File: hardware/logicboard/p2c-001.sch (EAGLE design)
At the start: 44 parts, among them IC1 74LS07N, K1 G5V1, T1 2SC1815

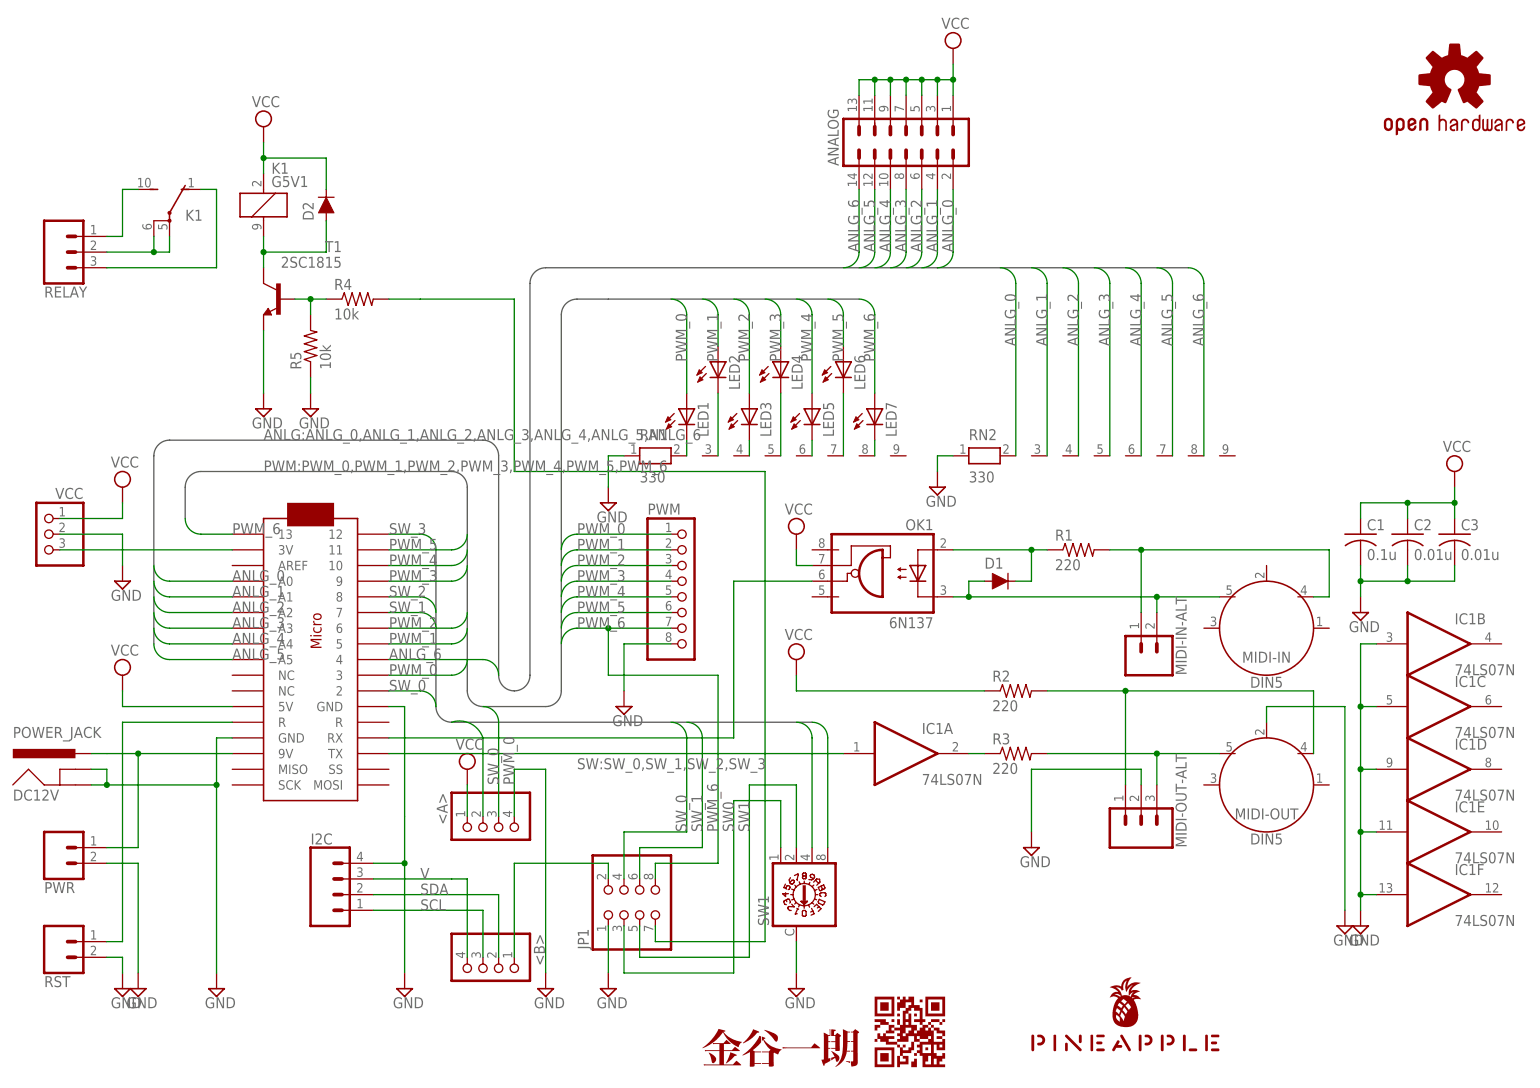
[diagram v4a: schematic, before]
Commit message: Changed DC jack and alternative connectors.
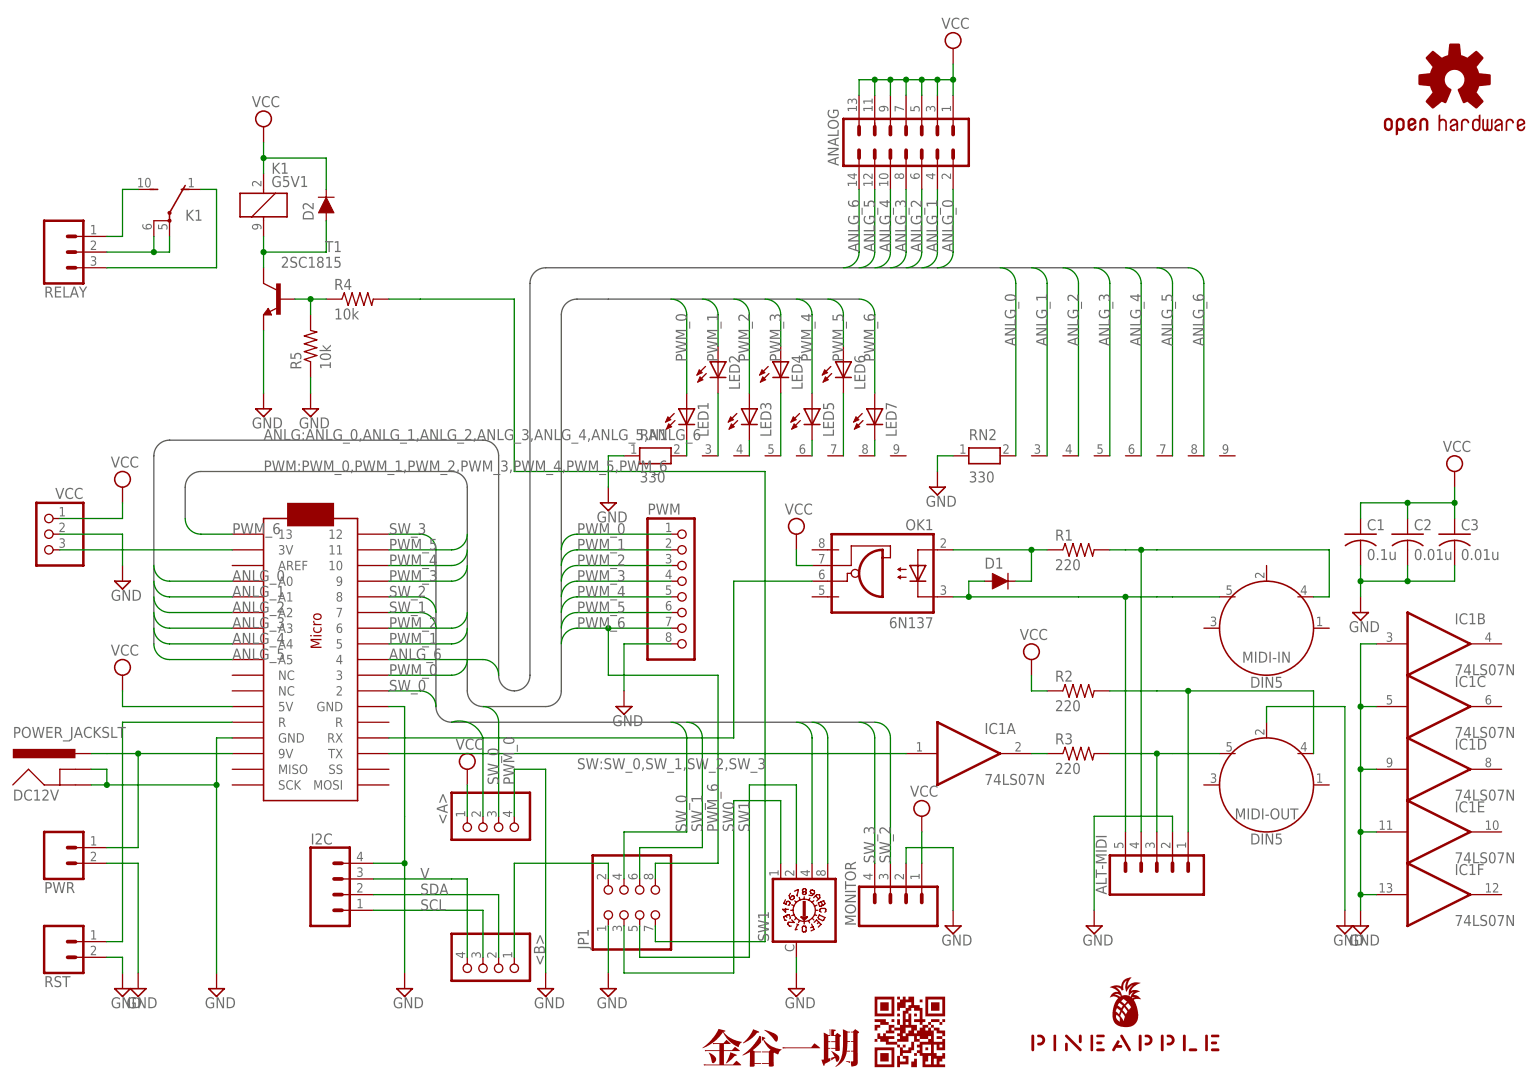
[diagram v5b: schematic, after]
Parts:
- removed MIDI-IN-ALT: (no value), SparkFun-Connectors:CONN_02JST-PTH-2
- removed MIDI-OUT-ALT: (no value), SparkFun-Connectors:CONN_03JST-PTH
- added ALT-MIDI: (no value), SparkFun-Connectors:CONN_05JST
- added MONITOR: (no value), SparkFun-Connectors:CONN_041.27MM
- DC12V: value POWER_JACK -> POWER_JACKSLT; device SparkFun-Connectors:POWER_JACK -> SparkFun-Connectors:POWER_JACKSLT
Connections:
- net GND: now also ALT-MIDI.2, MONITOR.2; no longer MIDI-OUT-ALT.2
- net MIDIIN+: now also ALT-MIDI.4; no longer MIDI-IN-ALT.1
- net MIDIIN-: now also ALT-MIDI.5; no longer MIDI-IN-ALT.2
- net MIDIOUT+: now also ALT-MIDI.1; no longer MIDI-OUT-ALT.1
- net MIDIOUT-: now also ALT-MIDI.3; no longer MIDI-OUT-ALT.3
- net SW_2: now also MONITOR.3
- net SW_3: now also MONITOR.4
- net VCC: now also MONITOR.1
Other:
- moved on the sheet: IC1A, R2, R3, SW1

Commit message: GND pad.
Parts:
- added GND: (no value), pinhead:PINHD-2X4
- MONITOR: device SparkFun-Connectors:CONN_041.27MM -> SparkFun-Connectors:CONN_04JST-PTH-VERT
- renumbered LED1 to L1, LED2 to L2, LED3 to L3, LED4 to L4, LED5 to L5, LED6 to L6, LED7 to L7
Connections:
- net GND: now also GND.1, GND.2, GND.3, GND.4, GND.5, GND.6, GND.7, GND.8
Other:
- moved on the sheet: C1, C2, C3

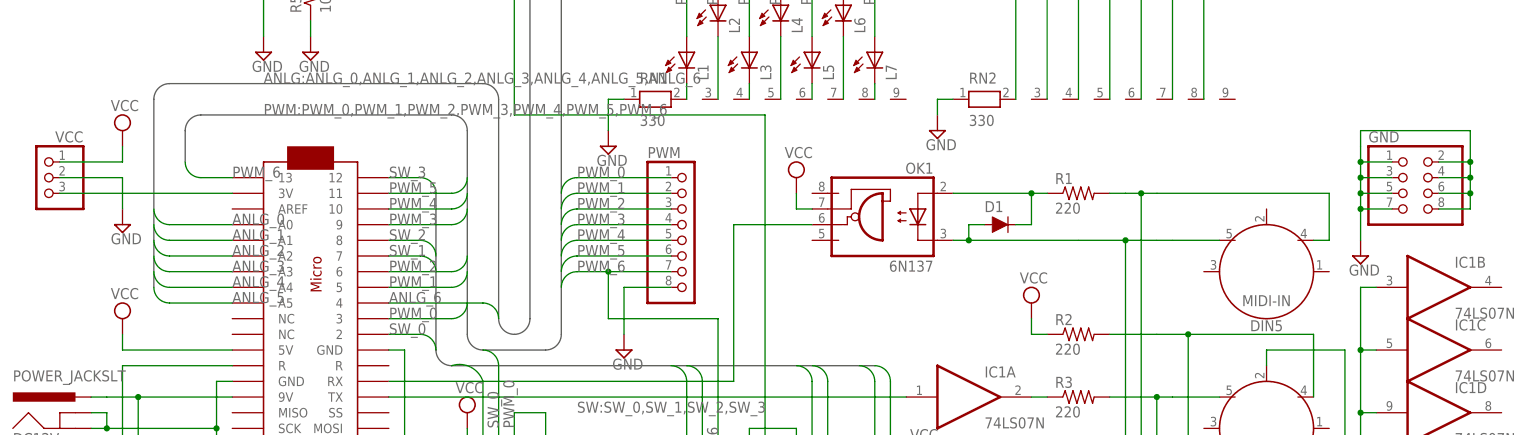
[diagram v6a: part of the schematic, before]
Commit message: Changed pinheaders to Sparkfan's ones.
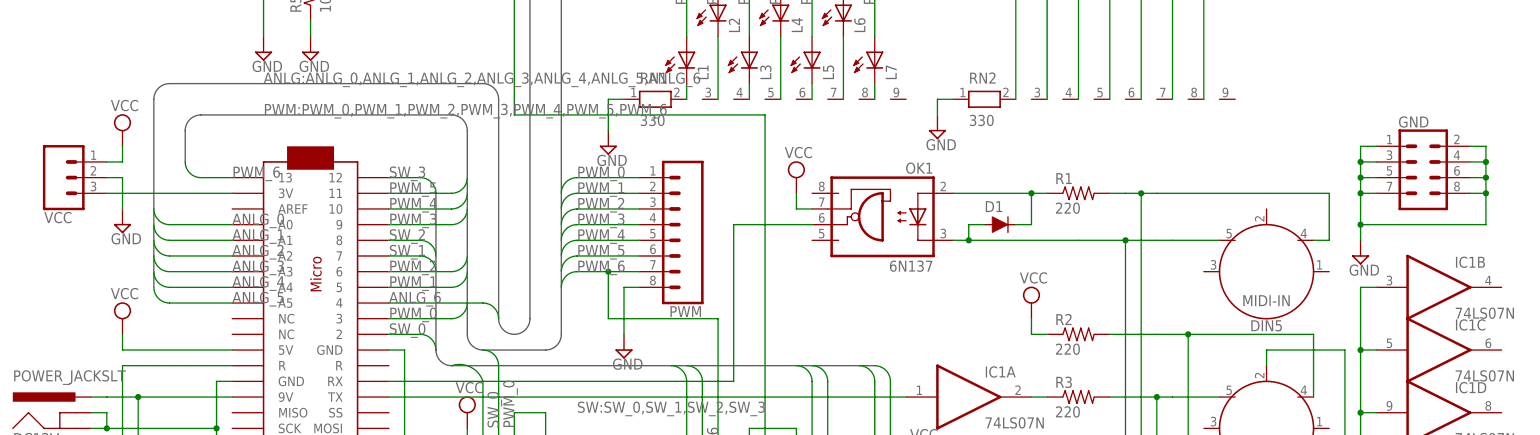
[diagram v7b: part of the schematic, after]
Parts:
- GND: device pinhead:PINHD-2X4 -> SparkFun-Connectors:CONN_04X2
- PWM: device pinhead:PINHD-1X8 -> SparkFun-Connectors:CONN_08"
- VCC: device pinhead:PINHD-1X3 -> SparkFun-Connectors:CONN_03

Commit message: Silk.
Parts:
- renumbered <A> to A, <B> to B
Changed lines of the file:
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@@
 <part name="SUPPLY23" library="supply2" library_urn="urn:adsk.eagle:library:372" deviceset="VCC" device=""/>
 <part name="RST" library="SparkFun-Connectors" library_urn="urn:adsk.eagle:library:513" deviceset="CONN_02" device="JST-PTH-2" package3d_urn="urn:adsk.eagle:package:38053/1"/>
-<part name="&lt;A&gt;" library="pinhead" library_urn="urn:adsk.eagle:library:325" deviceset="PINHD-1X4" device="" package3d_urn="urn:adsk.eagle:package:22407/2"/>
-<part name="&lt;B&gt;" library="pinhead" library_urn="urn:adsk.eagle:library:325" deviceset="PINHD-1X4" device="" package3d_urn="urn:adsk.eagle:package:22407/2"/>
+<part name="A" library="pinhead" library_urn="urn:adsk.eagle:library:325" deviceset="PINHD-1X4" device="" package3d_urn="urn:adsk.eagle:package:22407/2"/>
+<part name="B" library="pinhead" library_urn="urn:adsk.eagle:library:325" deviceset="PINHD-1X4" device="" package3d_urn="urn:adsk.eagle:package:22407/2"/>
 <part name="SUPPLY14" library="supply2" library_urn="urn:adsk.eagle:library:372" deviceset="GND" device=""/>
 <part name="JP1" library="pinhead" library_urn="urn:adsk.eagle:library:325" deviceset="PINHD-2X4" device="" package3d_urn="urn:adsk.eagle:package:22461/2"/>
@@
 <instance part="SUPPLY23" gate="G$1" x="48.26" y="157.48"/>
 <instance part="RST" gate="G$1" x="15.24" y="25.4" rot="MR180"/>
-<instance part="&lt;A&gt;" gate="A" x="86.36" y="43.18" rot="MR270"/>
-<instance part="&lt;B&gt;" gate="A" x="83.82" y="20.32" rot="R270"/>
+<instance part="A" gate="A" x="86.36" y="43.18" rot="MR270"/>
+<instance part="B" gate="A" x="83.82" y="20.32" rot="R270"/>
 <instance part="SUPPLY14" gate="GND" x="104.14" y="17.78"/>
 <instance part="JP1" gate="A" x="109.22" y="30.48" rot="R90"/>
@@
 </segment>
 <segment>
-<pinref part="&lt;A&gt;" gate="A" pin="4"/>
+<pinref part="A" gate="A" pin="4"/>
 <wire x1="88.9" y1="45.72" x2="88.9" y2="53.34" width="0.1524" layer="91"/>
 <pinref part="SUPPLY20" gate="GND" pin="GND"/>
@@
 <segment>
 <pinref part="SUPPLY19" gate="G$1" pin="VCC"/>
-<pinref part="&lt;A&gt;" gate="A" pin="1"/>
+<pinref part="A" gate="A" pin="1"/>
 <wire x1="81.28" y1="50.8" x2="81.28" y2="45.72" width="0.1524" layer="91"/>
 </segment>
@@
 </segment>
 <segment>
-<pinref part="&lt;A&gt;" gate="A" pin="2"/>
+<pinref part="A" gate="A" pin="2"/>
 <wire x1="78.74" y1="60.96" x2="83.82" y2="58.42" width="0.1524" layer="91" curve="-90"/>
 <wire x1="83.82" y1="58.42" x2="83.82" y2="45.72" width="0.1524" layer="91"/>
@@
 </segment>
 <segment>
-<pinref part="&lt;A&gt;" gate="A" pin="3"/>
+<pinref part="A" gate="A" pin="3"/>
 <wire x1="83.82" y1="63.5" x2="86.36" y2="60.96" width="0.1524" layer="91" curve="-90"/>
 <wire x1="86.36" y1="60.96" x2="86.36" y2="45.72" width="0.1524" layer="91"/>
@@
 <net name="I2CENABLE" class="0">
 <segment>
-<pinref part="&lt;B&gt;" gate="A" pin="1"/>
+<pinref part="B" gate="A" pin="1"/>
 <wire x1="88.9" y1="22.86" x2="88.9" y2="38.1" width="0.1524" layer="91"/>
 <wire x1="88.9" y1="38.1" x2="104.14" y2="38.1" width="0.1524" layer="91"/>
@@
 <net name="SDA" class="0">
 <segment>
-<pinref part="&lt;B&gt;" gate="A" pin="2"/>
+<pinref part="B" gate="A" pin="2"/>
 <wire x1="86.36" y1="22.86" x2="86.36" y2="33.02" width="0.1524" layer="91"/>
 <pinref part="I2C" gate="G$1" pin="2"/>
@@
 <net name="SCL" class="0">
 <segment>
-<pinref part="&lt;B&gt;" gate="A" pin="3"/>
+<pinref part="B" gate="A" pin="3"/>
 <wire x1="83.82" y1="22.86" x2="83.82" y2="30.48" width="0.1524" layer="91"/>
 <pinref part="I2C" gate="G$1" pin="1"/>
@@
 <pinref part="I2C" gate="G$1" pin="3"/>
 <wire x1="66.04" y1="35.56" x2="78.74" y2="35.56" width="0.1524" layer="91"/>
-<pinref part="&lt;B&gt;" gate="A" pin="4"/>
+<pinref part="B" gate="A" pin="4"/>
 <wire x1="78.74" y1="35.56" x2="81.28" y2="35.56" width="0.1524" layer="91"/>
 <wire x1="81.28" y1="35.56" x2="81.28" y2="22.86" width="0.1524" layer="91"/>
